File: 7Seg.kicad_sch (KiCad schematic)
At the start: 17 parts, among them Q901 SMMBT4403LT1G, Q902 SMMBT4403LT1G, Q903 SMMBT4403LT1G, Q904 SMMBT4403LT1G

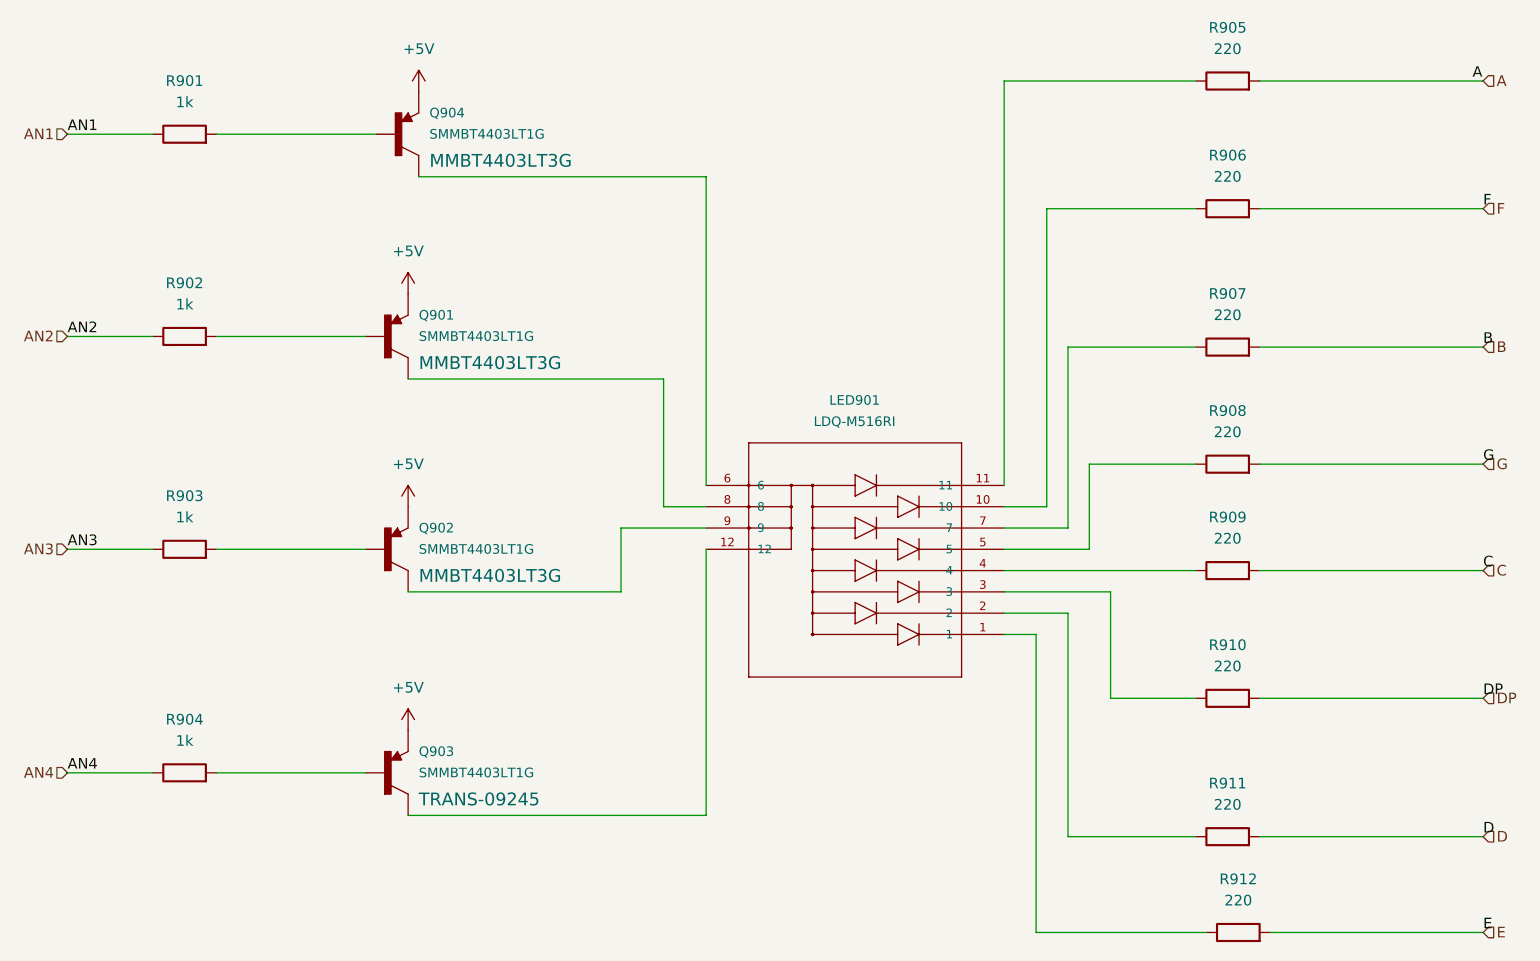
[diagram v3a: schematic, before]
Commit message: Fixed 7seg display
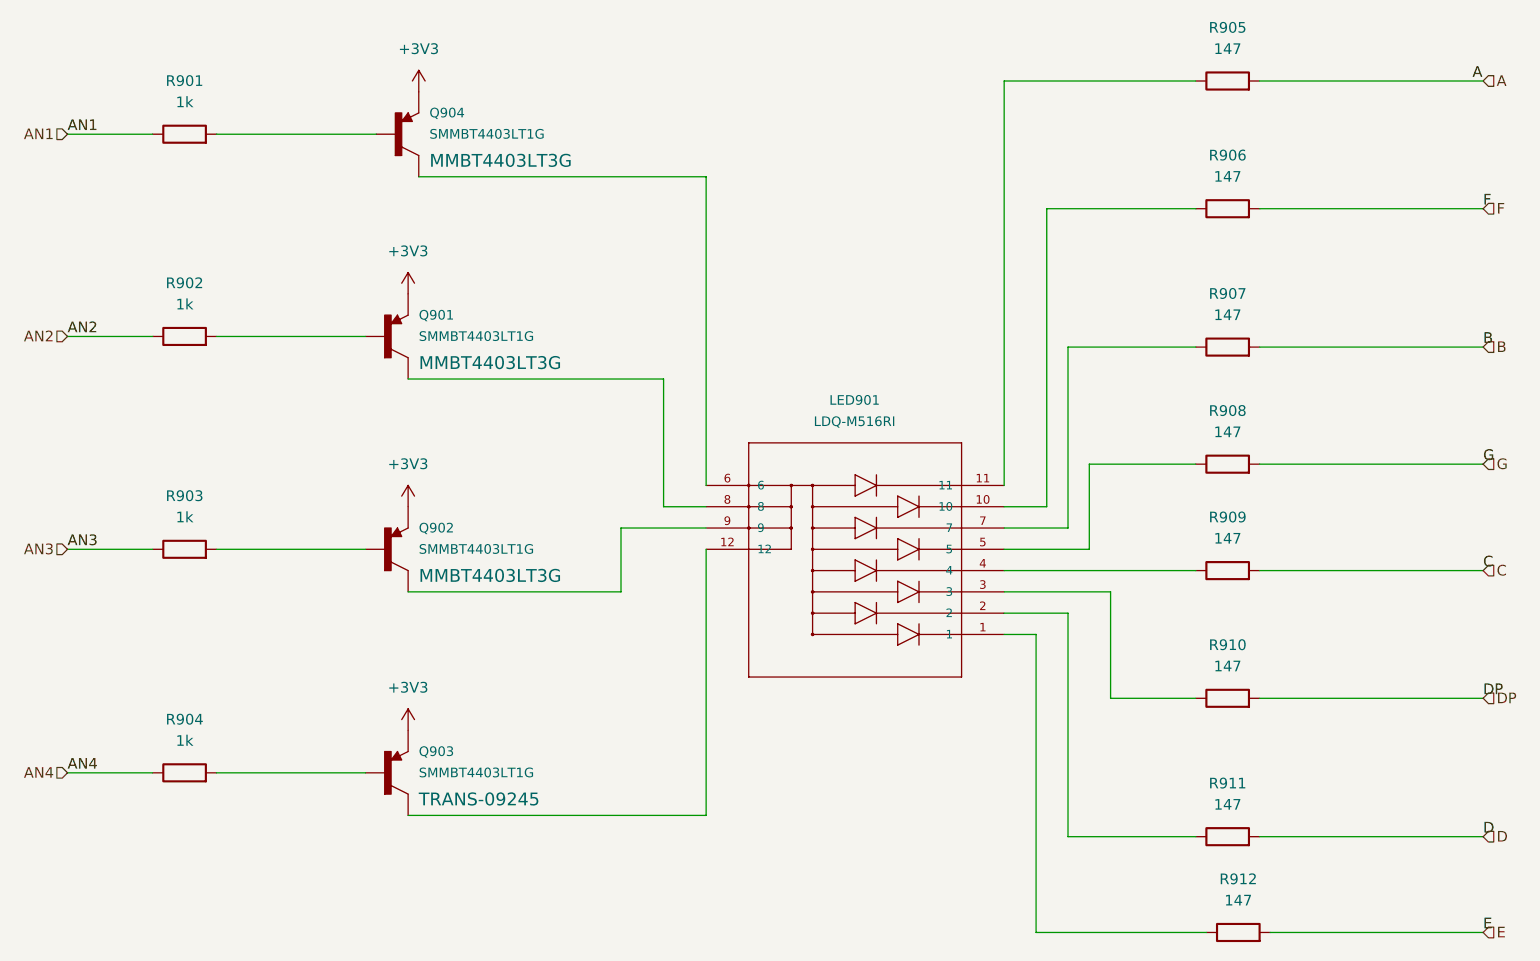
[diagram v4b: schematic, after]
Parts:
- R905, R906, R907, R908, R909, R910, R911, R912: value 220 -> 147
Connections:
- net +5V renamed +3V3
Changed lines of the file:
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@@
     (pin "9")
   )
+  (symbol (lib_id "power:+3V3") (at 92.71 97.79 0) (unit 1)
+    (in_bom yes) (on_board yes) (fields_autoplaced)
+    (property "Reference" "#PWR0141" (id 0) (at 92.71 101.6 0)
+      (effects (font (size 1.27 1.27)) hide)
+    )
+    (property "Value" "+3V3" (id 1) (at 92.71 92.71 0))
+    (property "Footprint" "" (id 2) (at 92.71 97.79 0)
+      (effects (font (size 1.27 1.27)) hide)
+    )
+    (property "Datasheet" "" (id 3) (at 92.71 97.79 0)
+      (effects (font (size 1.27 1.27)) hide)
+    )
+    (pin "1")
+  )
   (symbol (lib_id "Device:R") (at 191.77 148.59 90) (unit 1)
     (in_bom yes) (on_board yes) (fields_autoplaced)
     (property "Reference" "R912" (id 0) (at 191.77 142.24 90))
-    (property "Value" "220" (id 1) (at 191.77 144.78 90))
+    (property "Value" "147" (id 1) (at 191.77 144.78 90))
     (property "Footprint" "Resistor_SMD:R_0603_1608Metric" (id 2) (at 191.77 150.368 90)
       (effects (font (size 1.27 1.27)) hide)
@@
     (pin "1")
     (pin "2")
-  )
-  (symbol (lib_id "power:+5V") (at 92.71 124.46 0) (unit 1)
-    (in_bom yes) (on_board yes) (fields_autoplaced)
-    (property "Reference" "#PWR0903" (id 0) (at 92.71 128.27 0)
-      (effects (font (size 1.27 1.27)) hide)
-    )
-    (property "Value" "+5V" (id 1) (at 92.71 119.38 0))
-    (property "Footprint" "" (id 2) (at 92.71 124.46 0)
-      (effects (font (size 1.27 1.27)) hide)
-    )
-    (property "Datasheet" "" (id 3) (at 92.71 124.46 0)
-      (effects (font (size 1.27 1.27)) hide)
-    )
-    (pin "1")
   )
   (symbol (lib_id "SparkFun-DiscreteSemi:TRANS_PNP-MMBT4403") (at 91.44 53.34 0) (unit 1)
@@
     (in_bom yes) (on_board yes) (fields_autoplaced)
     (property "Reference" "R911" (id 0) (at 190.5 130.81 90))
-    (property "Value" "220" (id 1) (at 190.5 133.35 90))
+    (property "Value" "147" (id 1) (at 190.5 133.35 90))
     (property "Footprint" "Resistor_SMD:R_0603_1608Metric" (id 2) (at 190.5 138.938 90)
       (effects (font (size 1.27 1.27)) hide)
@@
     (pin "2")
   )
+  (symbol (lib_id "power:+3V3") (at 92.71 124.46 0) (unit 1)
+    (in_bom yes) (on_board yes) (fields_autoplaced)
+    (property "Reference" "#PWR0140" (id 0) (at 92.71 128.27 0)
+      (effects (font (size 1.27 1.27)) hide)
+    )
+    (property "Value" "+3V3" (id 1) (at 92.71 119.38 0))
+    (property "Footprint" "" (id 2) (at 92.71 124.46 0)
+      (effects (font (size 1.27 1.27)) hide)
+    )
+    (property "Datasheet" "" (id 3) (at 92.71 124.46 0)
+      (effects (font (size 1.27 1.27)) hide)
+    )
+    (pin "1")
+  )
+  (symbol (lib_id "power:+3V3") (at 92.71 72.39 0) (unit 1)
+    (in_bom yes) (on_board yes) (fields_autoplaced)
+    (property "Reference" "#PWR0142" (id 0) (at 92.71 76.2 0)
+      (effects (font (size 1.27 1.27)) hide)
+    )
+    (property "Value" "+3V3" (id 1) (at 92.71 67.31 0))
+    (property "Footprint" "" (id 2) (at 92.71 72.39 0)
+      (effects (font (size 1.27 1.27)) hide)
+    )
+    (property "Datasheet" "" (id 3) (at 92.71 72.39 0)
+      (effects (font (size 1.27 1.27)) hide)
+    )
+    (pin "1")
+  )
   (symbol (lib_id "Device:R") (at 190.5 78.74 90) (unit 1)
     (in_bom yes) (on_board yes) (fields_autoplaced)
     (property "Reference" "R907" (id 0) (at 190.5 72.39 90))
-    (property "Value" "220" (id 1) (at 190.5 74.93 90))
+    (property "Value" "147" (id 1) (at 190.5 74.93 90))
     (property "Footprint" "Resistor_SMD:R_0603_1608Metric" (id 2) (at 190.5 80.518 90)
       (effects (font (size 1.27 1.27)) hide)
@@
     (pin "3")
   )
-  (symbol (lib_id "power:+5V") (at 93.98 48.26 0) (unit 1)
-    (in_bom yes) (on_board yes) (fields_autoplaced)
-    (property "Reference" "#PWR0904" (id 0) (at 93.98 52.07 0)
-      (effects (font (size 1.27 1.27)) hide)
-    )
-    (property "Value" "+5V" (id 1) (at 93.98 43.18 0))
-    (property "Footprint" "" (id 2) (at 93.98 48.26 0)
-      (effects (font (size 1.27 1.27)) hide)
-    )
-    (property "Datasheet" "" (id 3) (at 93.98 48.26 0)
-      (effects (font (size 1.27 1.27)) hide)
-    )
-    (pin "1")
-  )
   (symbol (lib_id "Device:R") (at 66.04 129.54 90) (unit 1)
     (in_bom yes) (on_board yes) (fields_autoplaced)
@@
     (pin "3")
   )
-  (symbol (lib_id "power:+5V") (at 92.71 72.39 0) (unit 1)
-    (in_bom yes) (on_board yes) (fields_autoplaced)
-    (property "Reference" "#PWR0901" (id 0) (at 92.71 76.2 0)
-      (effects (font (size 1.27 1.27)) hide)
-    )
-    (property "Value" "+5V" (id 1) (at 92.71 67.31 0))
-    (property "Footprint" "" (id 2) (at 92.71 72.39 0)
-      (effects (font (size 1.27 1.27)) hide)
-    )
-    (property "Datasheet" "" (id 3) (at 92.71 72.39 0)
+  (symbol (lib_id "power:+3V3") (at 93.98 48.26 0) (unit 1)
+    (in_bom yes) (on_board yes) (fields_autoplaced)
+    (property "Reference" "#PWR0143" (id 0) (at 93.98 52.07 0)
+      (effects (font (size 1.27 1.27)) hide)
+    )
+    (property "Value" "+3V3" (id 1) (at 93.98 43.18 0))
+    (property "Footprint" "" (id 2) (at 93.98 48.26 0)
+      (effects (font (size 1.27 1.27)) hide)
+    )
+    (property "Datasheet" "" (id 3) (at 93.98 48.26 0)
       (effects (font (size 1.27 1.27)) hide)
     )
@@
     (in_bom yes) (on_board yes) (fields_autoplaced)
     (property "Reference" "R906" (id 0) (at 190.5 55.88 90))
-    (property "Value" "220" (id 1) (at 190.5 58.42 90))
+    (property "Value" "147" (id 1) (at 190.5 58.42 90))
     (property "Footprint" "Resistor_SMD:R_0603_1608Metric" (id 2) (at 190.5 64.008 90)
       (effects (font (size 1.27 1.27)) hide)
@@
     (pin "3")
   )
-  (symbol (lib_id "power:+5V") (at 92.71 97.79 0) (unit 1)
-    (in_bom yes) (on_board yes) (fields_autoplaced)
-    (property "Reference" "#PWR0902" (id 0) (at 92.71 101.6 0)
-      (effects (font (size 1.27 1.27)) hide)
-    )
-    (property "Value" "+5V" (id 1) (at 92.71 92.71 0))
-    (property "Footprint" "" (id 2) (at 92.71 97.79 0)
-      (effects (font (size 1.27 1.27)) hide)
-    )
-    (property "Datasheet" "" (id 3) (at 92.71 97.79 0)
-      (effects (font (size 1.27 1.27)) hide)
-    )
-    (pin "1")
-  )
   (symbol (lib_id "Device:R") (at 190.5 120.65 90) (unit 1)
     (in_bom yes) (on_board yes) (fields_autoplaced)
     (property "Reference" "R910" (id 0) (at 190.5 114.3 90))
-    (property "Value" "220" (id 1) (at 190.5 116.84 90))
+    (property "Value" "147" (id 1) (at 190.5 116.84 90))
     (property "Footprint" "Resistor_SMD:R_0603_1608Metric" (id 2) (at 190.5 122.428 90)
       (effects (font (size 1.27 1.27)) hide)
@@
     (in_bom yes) (on_board yes) (fields_autoplaced)
     (property "Reference" "R905" (id 0) (at 190.5 40.64 90))
-    (property "Value" "220" (id 1) (at 190.5 43.18 90))
+    (property "Value" "147" (id 1) (at 190.5 43.18 90))
     (property "Footprint" "Resistor_SMD:R_0603_1608Metric" (id 2) (at 190.5 48.768 90)
       (effects (font (size 1.27 1.27)) hide)
@@
     (in_bom yes) (on_board yes) (fields_autoplaced)
     (property "Reference" "R908" (id 0) (at 190.5 86.36 90))
-    (property "Value" "220" (id 1) (at 190.5 88.9 90))
+    (property "Value" "147" (id 1) (at 190.5 88.9 90))
     (property "Footprint" "Resistor_SMD:R_0603_1608Metric" (id 2) (at 190.5 94.488 90)
       (effects (font (size 1.27 1.27)) hide)
@@
     (in_bom yes) (on_board yes) (fields_autoplaced)
     (property "Reference" "R909" (id 0) (at 190.5 99.06 90))
-    (property "Value" "220" (id 1) (at 190.5 101.6 90))
+    (property "Value" "147" (id 1) (at 190.5 101.6 90))
     (property "Footprint" "Resistor_SMD:R_0603_1608Metric" (id 2) (at 190.5 107.188 90)
       (effects (font (size 1.27 1.27)) hide)
